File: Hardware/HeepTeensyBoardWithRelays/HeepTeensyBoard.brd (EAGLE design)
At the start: 100 x 80 mm, 43 parts, among them J1 MAGJACK, J4 POWER_JACKPTH, K1 RELAY-SPDT-JZC-11F, K2 RELAY-SPDT-JZC-11F, K3 RELAY-SPDT-JZC-11F, Q1 25MHz, U1 ENC28J60-SO

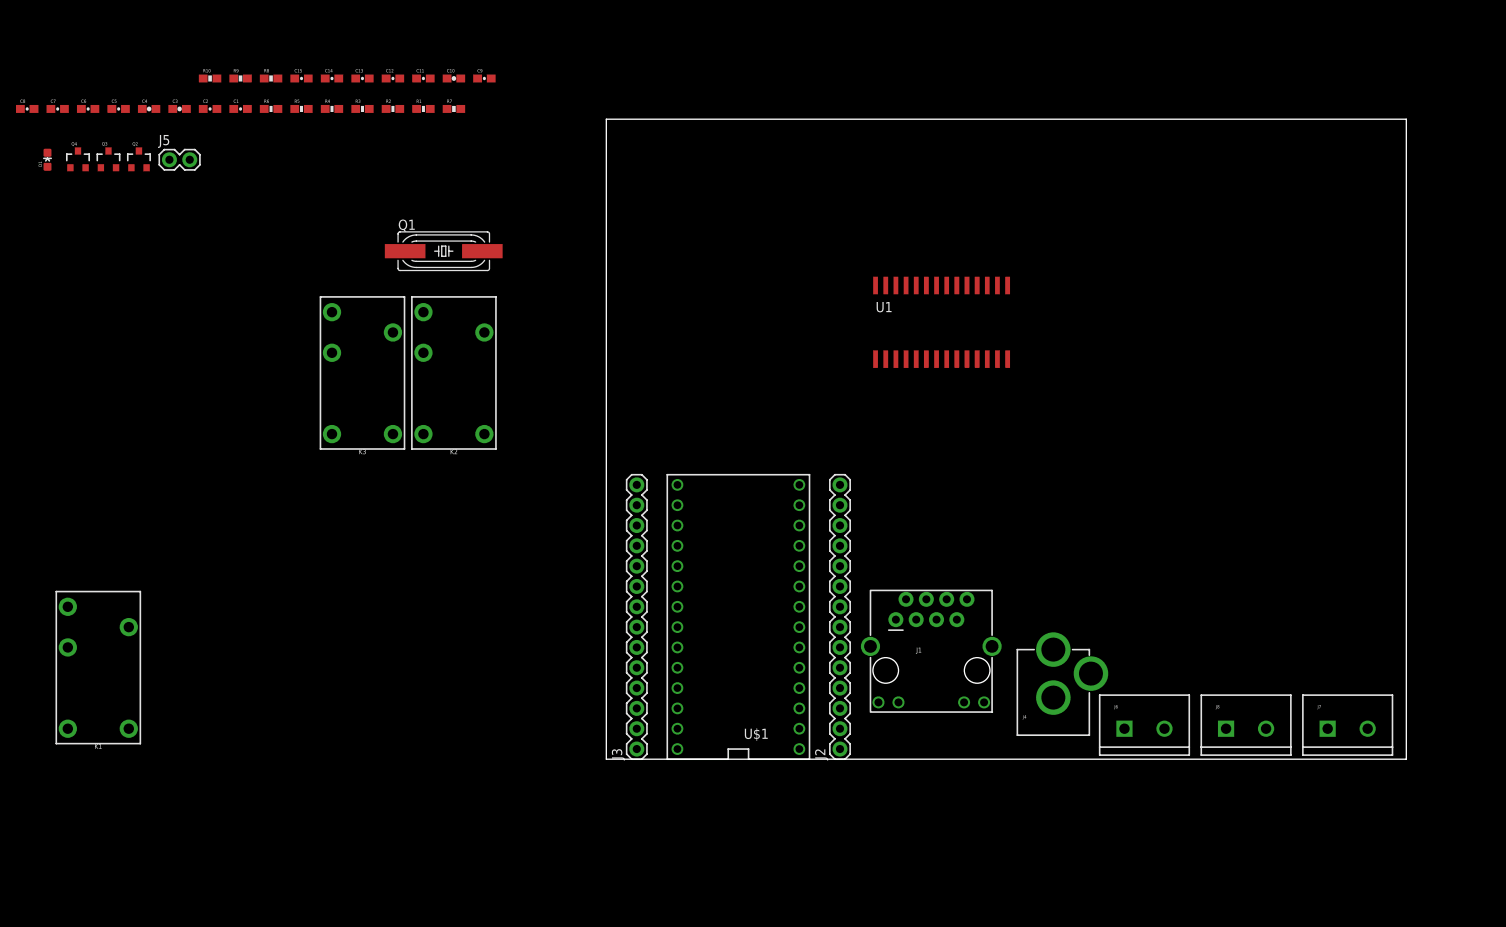
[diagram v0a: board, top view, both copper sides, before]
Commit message: #152 Move all components to the board
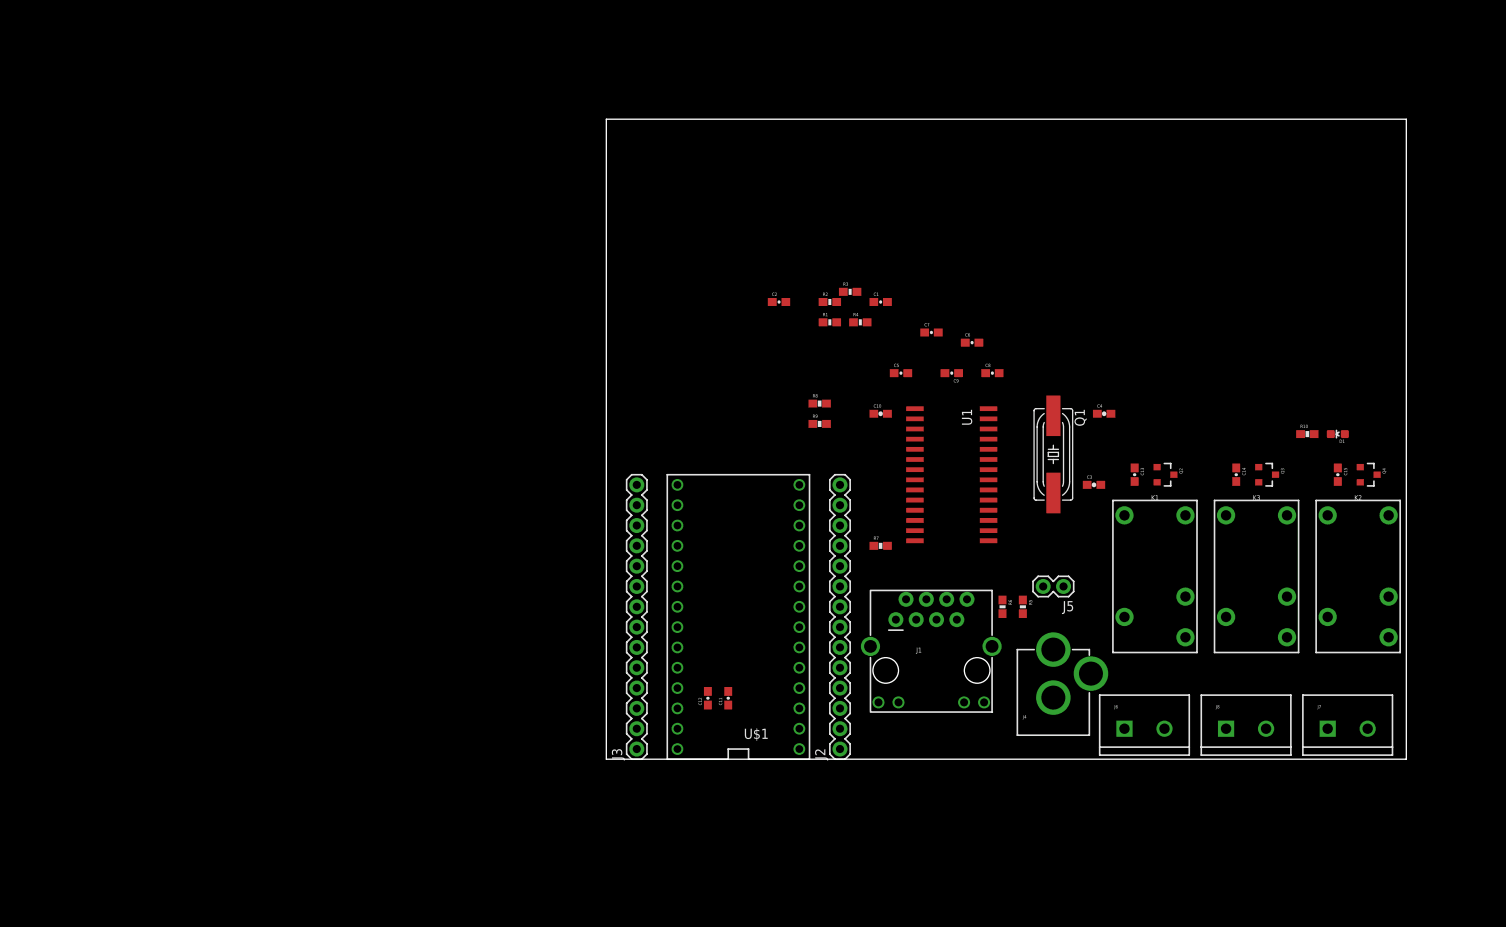
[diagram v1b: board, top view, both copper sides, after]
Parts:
- moved Q4 166.0 mm to (95.2, 35.6), turned to 270 degrees
- moved D1 164.9 mm to (91.4, 40.6), turned to 90 degrees
- moved Q3 150.0 mm to (82.5, 35.6), turned to 270 degrees
- moved R10 144.2 mm to (87.6, 40.6)
- moved C15 138.7 mm to (91.4, 35.6), turned to 270 degrees
- moved Q2 134.2 mm to (69.8, 35.6), turned to 270 degrees
- moved K1 132.4 mm to (68.6, 21.6), turned to 180 degrees
- moved C4 125.3 mm to (62.2, 43.2)
- moved C8 125.1 mm to (48.3, 48.3)
- moved J5 123.8 mm to (57.1, 21.6), turned to 180 degrees
- moved C3 123.6 mm to (61.0, 34.3)
- moved C14 123.4 mm to (78.7, 35.6), turned to 270 degrees
- moved K2 116.4 mm to (94.0, 21.6), turned to 180 degrees
- moved K3 115.2 mm to (81.3, 21.6), turned to 180 degrees
- moved C6 114.3 mm to (45.7, 52.1)
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
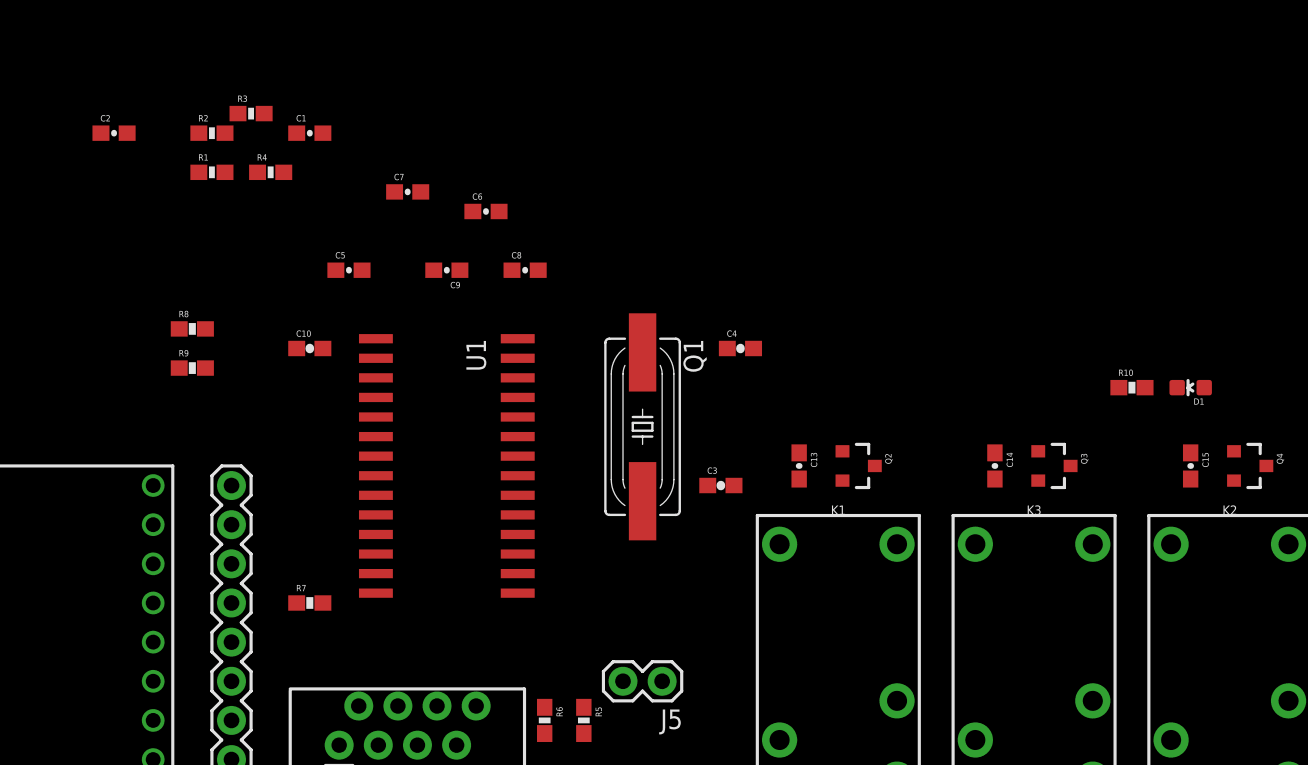
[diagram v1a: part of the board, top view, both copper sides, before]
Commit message: #152 Laid parts out on circuit board
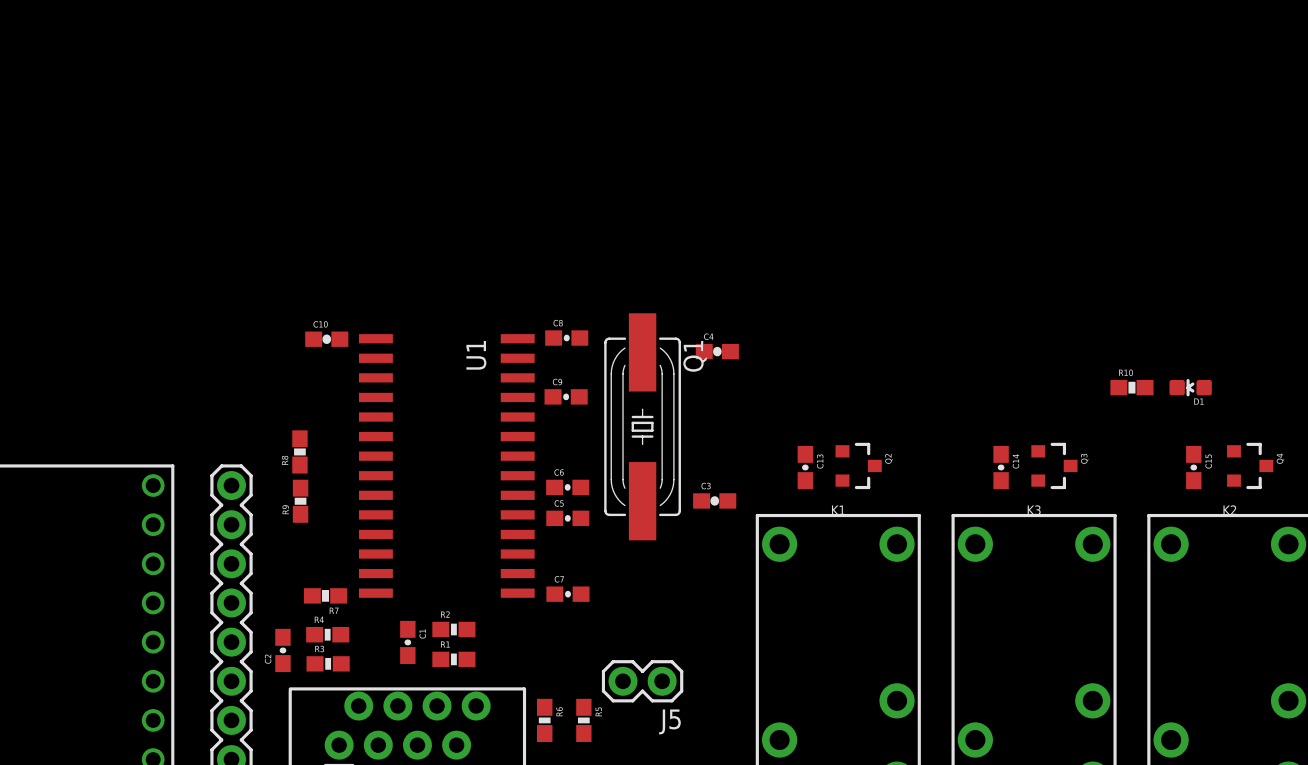
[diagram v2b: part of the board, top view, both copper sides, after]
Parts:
- moved R3 36.0 mm to (35.5, 22.7)
- moved R2 35.8 mm to (43.6, 24.9)
- moved C2 35.3 mm to (32.5, 23.6), turned to 90 degrees
- moved R1 35.3 mm to (43.6, 23.0)
- moved C1 33.6 mm to (40.6, 24.1), turned to 270 degrees
- moved R4 30.2 mm to (35.5, 24.6)
- moved C7 28.1 mm to (51.0, 27.2)
- moved C5 21.5 mm to (51.0, 32.2)
- moved C6 18.7 mm to (51.0, 34.2)
- moved C9 11.3 mm to (50.9, 40.0), turned to 0 degrees
- moved R9 11.1 mm to (33.7, 33.3), turned to 90 degrees
- moved R8 10.6 mm to (33.6, 36.5), turned to 90 degrees
- moved C8 5.16 mm to (51.0, 43.9)
- moved C4 1.51 mm to (60.7, 43.0)
- moved C10 1.25 mm to (35.4, 43.8)
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
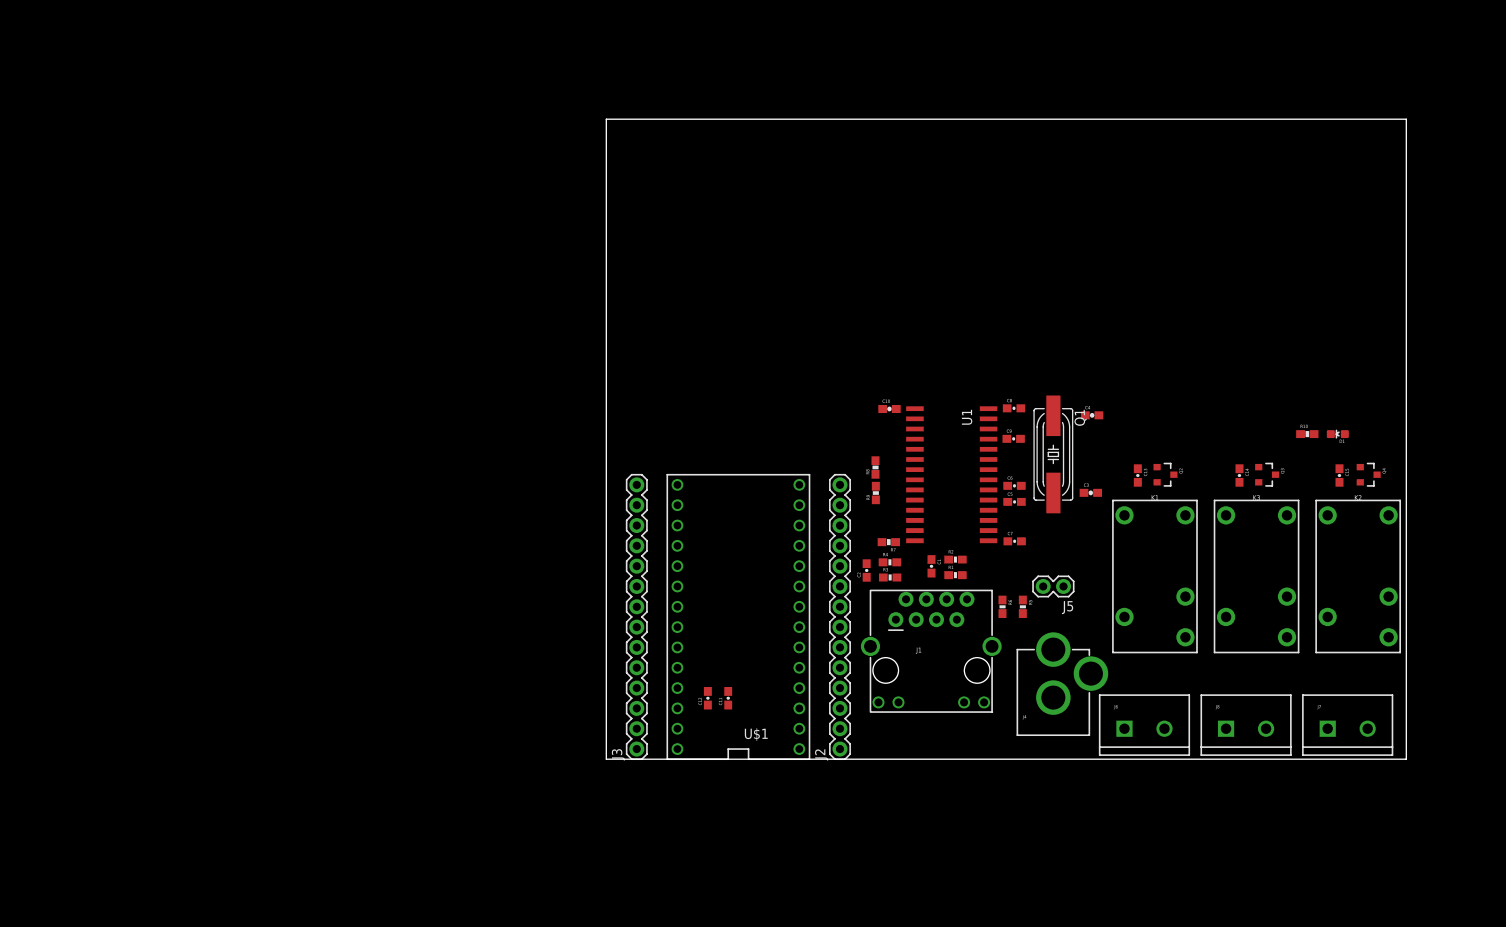
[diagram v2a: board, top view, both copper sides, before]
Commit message: #152 Routed The relay board
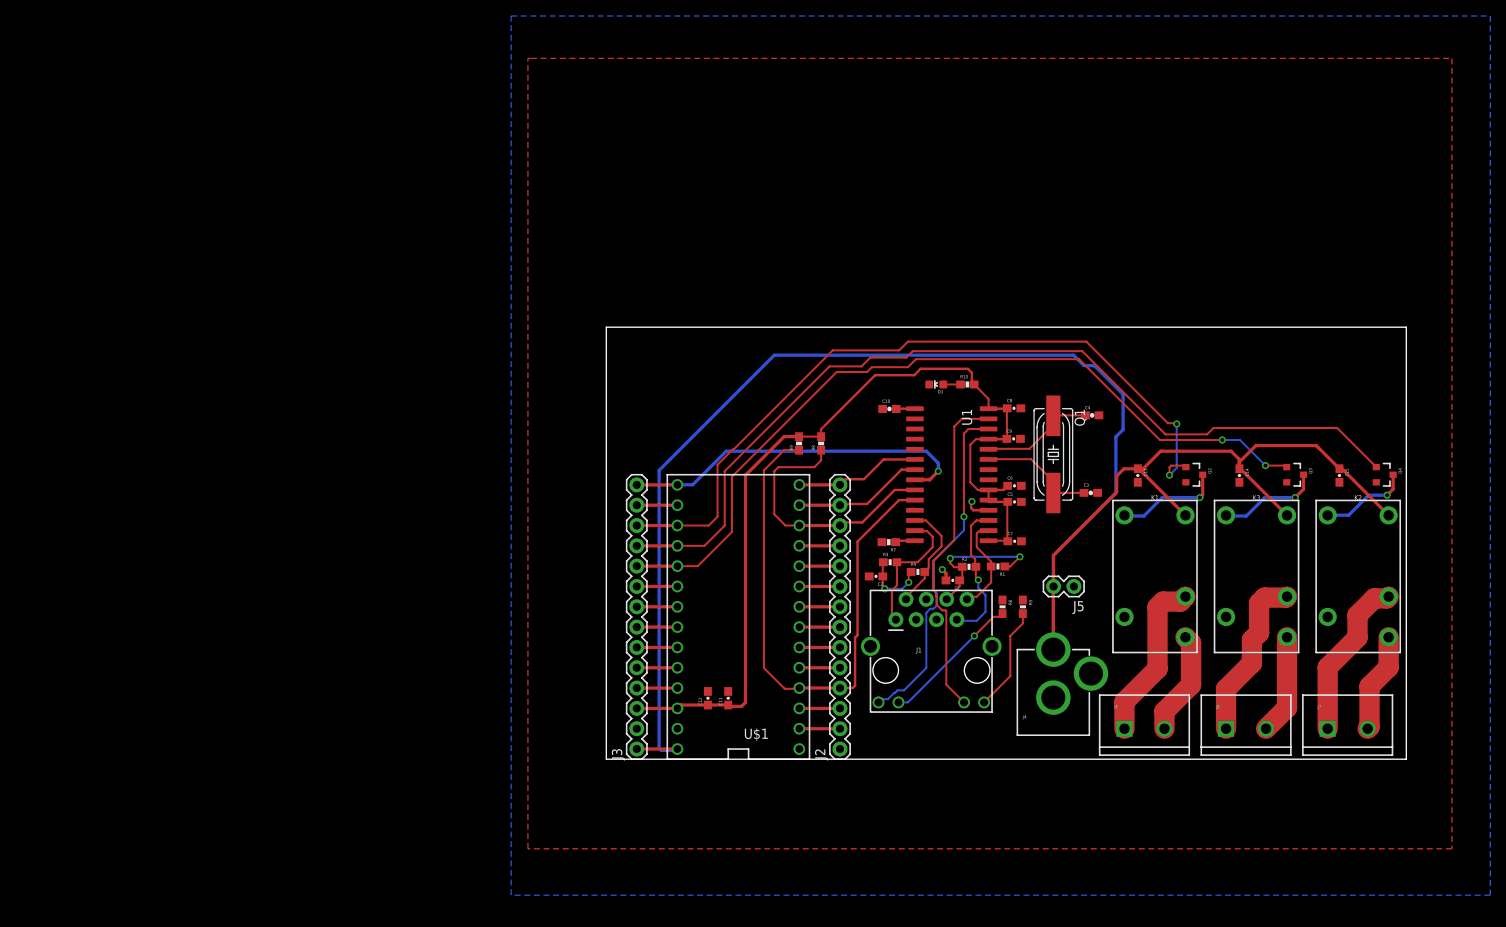
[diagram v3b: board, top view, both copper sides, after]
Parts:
- moved D1 50.6 mm to (41.2, 46.8)
- moved R10 42.9 mm to (45.1, 46.8)
- moved R9 11.4 mm to (24.1, 39.5)
- moved R8 7.43 mm to (26.9, 39.5)
- moved R1 5.43 mm to (49.0, 24.1), turned to 180 degrees
- moved R4 3.70 mm to (39.0, 23.4)
- moved Q2 3.60 mm to (73.5, 35.6)
- moved Q3 3.50 mm to (86.0, 35.6)
- moved C1 3.19 mm to (43.3, 22.4), turned to 180 degrees
- moved Q4 2.00 mm to (97.2, 35.6)
- moved R2 1.92 mm to (45.3, 24.1)
- moved R3 1.90 mm to (35.5, 24.6)
- moved C2 1.38 mm to (33.7, 22.9), turned to 180 degrees
- moved J5 1.30 mm to (58.5, 21.6)
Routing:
- net VIN: track 0.00 -> 227.3 mm
- net 3.3V: track 0.00 -> 114.6 mm
- net TEENSY16: track 0.00 -> 113.2 mm
- net TEENSY17: track 0.00 -> 101.6 mm, vias 0 -> 2
- net TEENSY15: track 0.00 -> 95.1 mm, vias 0 -> 2
- net #RESET: track 0.00 -> 70.2 mm
- net SCK: track 0.00 -> 45.4 mm, vias 0 -> 1
- net LEDB: track 0.00 -> 42.9 mm, vias 0 -> 1
- net LEDA: track 0.00 -> 42.1 mm
- net #CS: track 0.00 -> 33.1 mm
- net N$21: track 0.00 -> 21.2 mm
- net N$16: track 0.00 -> 20.9 mm
- net N$19: track 0.00 -> 20.6 mm
- net N$7: track 0.00 -> 18.4 mm, vias 0 -> 2
- net N$4: track 0.00 -> 18.1 mm, vias 0 -> 1
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- added copper zone on layer 1, net GND
- added copper zone on layer 16, net GND
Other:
- board size 100 x 80 mm -> 100 x 54 mm

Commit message: #152 Finished last airwire
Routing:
- net GND: track 5.22 -> 15.8 mm, vias 2 -> 3
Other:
- board text added: "AC Relay Controller"
- board text added: "Device 1"
- board text added: "Device 2"
- board text added: "Device 3"
- board text added: "Heep I/O"
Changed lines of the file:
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@@
 <wire x1="100" y1="54" x2="0" y2="54" width="0" layer="20"/>
 <wire x1="0" y1="54" x2="0" y2="0" width="0" layer="20"/>
+<text x="64" y="9" size="1.778" layer="21">Device 1</text>
+<text x="76" y="9" size="1.778" layer="21">Device 2</text>
+<text x="88" y="9" size="1.778" layer="21">Device 3</text>
+<text x="69" y="47" size="3.81" layer="21">Heep I/O</text>
+<text x="68" y="43" size="1.9304" layer="21">AC Relay Controller</text>
 </plain>
 <attributes>
@@
 <via x="42" y="23.7" extent="1-16" drill="0.5" shape="square"/>
 <wire x1="42" y1="23.7" x2="42" y2="23.9" width="0.4064" layer="16"/>
-<wire x1="12.7" y1="8.47" x2="8.89" y2="3.81" width="0" layer="19" extent="1-1"/>
+<wire x1="8.89" y1="3.81" x2="9.81" y2="3.81" width="0.4064" layer="16"/>
+<wire x1="9.81" y1="3.81" x2="11" y2="5" width="0.4064" layer="16"/>
+<wire x1="11" y1="5" x2="11" y2="11" width="0.4064" layer="16"/>
+<via x="11" y="11" extent="1-16" drill="0.5" shape="square"/>
+<wire x1="11" y1="11" x2="13" y2="11" width="0.4064" layer="1"/>
 </signal>
 <signal name="LEDA">
